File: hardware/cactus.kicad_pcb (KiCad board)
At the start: 2 copper layers, 76.5 x 38.1 mm, 25 parts, among them SW1 SW_Push, U1 WeMos_Battery_Shield, U2 WeMos_D1_mini, U3 74HC595, U4 Si7021_breakout

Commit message: [bug] Remove extra via in R2. Fixed #10
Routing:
- net Net-(D2-Pad2): vias 2 -> 1
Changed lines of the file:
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@@
     (thickness 1.6)
     (drawings 36)
-    (tracks 179)
+    (tracks 178)
     (zones 0)
     (modules 25)
@@
   (layers
     (0 F.Cu signal)
-    (31 B.Cu signal hide)
-    (32 B.Adhes user hide)
+    (31 B.Cu signal)
+    (32 B.Adhes user)
     (33 F.Adhes user)
-    (34 B.Paste user hide)
+    (34 B.Paste user)
     (35 F.Paste user)
-    (36 B.SilkS user hide)
+    (36 B.SilkS user)
     (37 F.SilkS user)
-    (38 B.Mask user hide)
-    (39 F.Mask user hide)
-    (40 Dwgs.User user hide)
-    (41 Cmts.User user hide)
+    (38 B.Mask user)
+    (39 F.Mask user)
+    (40 Dwgs.User user)
+    (41 Cmts.User user)
     (42 Eco1.User user)
     (43 Eco2.User user)
@@
   (segment (start 151.511 55.499) (end 151.638 55.626) (width 0.25) (layer F.Cu) (net 5))
   (segment (start 151.511 54.102) (end 151.511 55.499) (width 0.25) (layer F.Cu) (net 5))
-  (via (at 151.62 56.896) (size 0.8) (drill 0.4) (layers F.Cu B.Cu) (net 5))
   (segment (start 151.638 56.878) (end 151.62 56.896) (width 0.25) (layer B.Cu) (net 5))
   (segment (start 151.638 55.626) (end 151.638 56.878) (width 0.25) (layer B.Cu) (net 5))
@@
     (connect_pads (clearance 0.508))
     (min_thickness 0.254)
-    (fill (arc_segments 16) (thermal_gap 0.508) (thermal_bridge_width 0.508))
+    (fill yes (arc_segments 16) (thermal_gap 0.508) (thermal_bridge_width 0.508))
     (polygon
       (pts
@@
     (connect_pads (clearance 0.508))
     (min_thickness 0.254)
-    (fill (arc_segments 16) (thermal_gap 0.508) (thermal_bridge_width 0.508))
+    (fill yes (arc_segments 16) (thermal_gap 0.508) (thermal_bridge_width 0.508))
     (polygon
       (pts

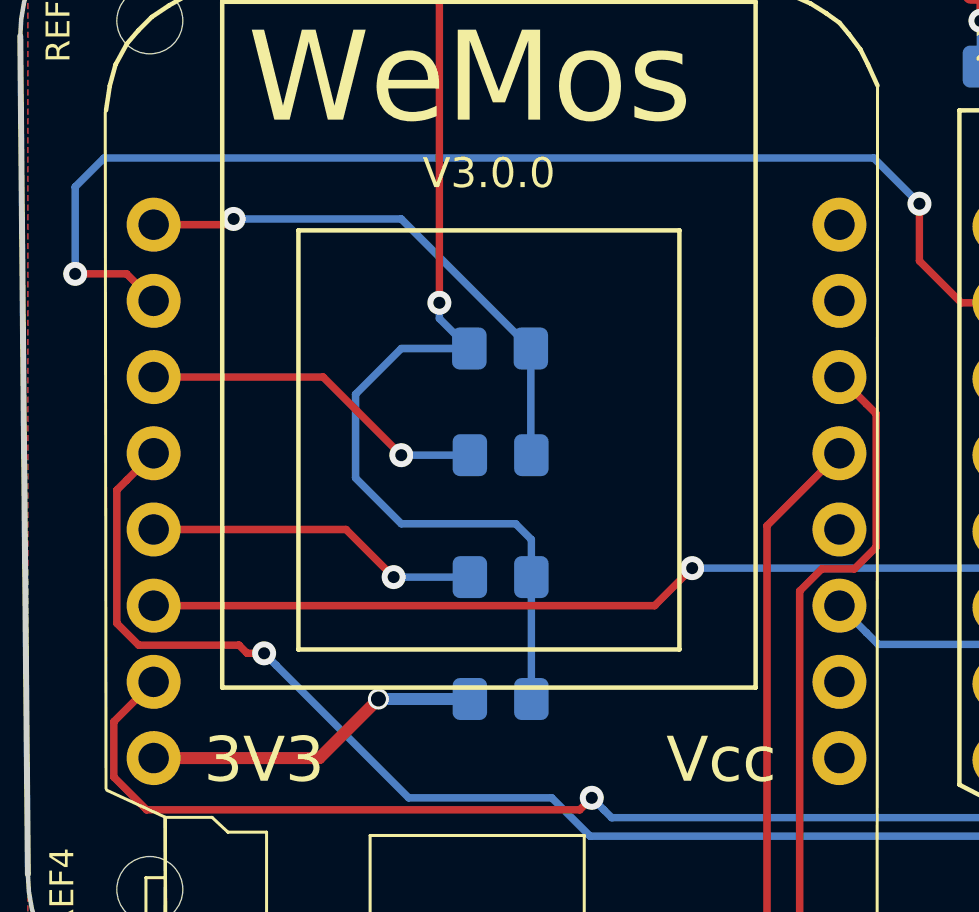
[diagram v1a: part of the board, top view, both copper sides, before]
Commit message: [footprint] Add more pin notes on silkscreen
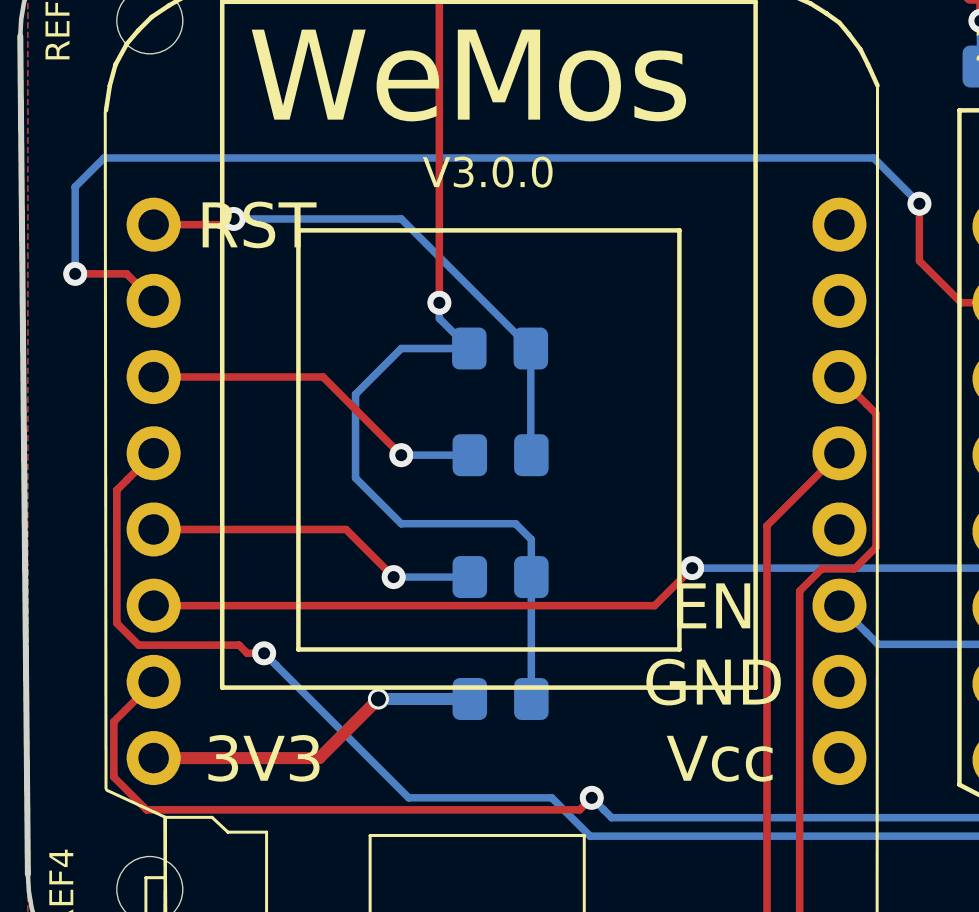
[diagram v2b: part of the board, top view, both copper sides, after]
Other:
- board text added: "EN"
- board text added: "RST"
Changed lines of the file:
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@@
   (general
     (thickness 1.6)
-    (drawings 36)
+    (drawings 39)
     (tracks 178)
     (zones 0)
@@
   (layers
     (0 F.Cu signal)
-    (31 B.Cu signal)
-    (32 B.Adhes user)
+    (31 B.Cu signal hide)
+    (32 B.Adhes user hide)
     (33 F.Adhes user)
-    (34 B.Paste user)
+    (34 B.Paste user hide)
     (35 F.Paste user)
-    (36 B.SilkS user)
+    (36 B.SilkS user hide)
     (37 F.SilkS user)
-    (38 B.Mask user)
+    (38 B.Mask user hide)
     (39 F.Mask user)
     (40 Dwgs.User user)
-    (41 Cmts.User user)
+    (41 Cmts.User user hide)
     (42 Eco1.User user)
     (43 Eco2.User user)
     (44 Edge.Cuts user)
     (45 Margin user)
-    (46 B.CrtYd user)
+    (46 B.CrtYd user hide)
     (47 F.CrtYd user)
-    (48 B.Fab user)
+    (48 B.Fab user hide)
     (49 F.Fab user)
   )
@@
     (pad 1 np_thru_hole circle (at 0 0) (size 2.2 2.2) (drill 2.2) (layers *.Cu *.Mask))
   )
+  (gr_text RST (at 121.92 62.23) (layer F.SilkS)
+    (effects (font (size 1.5 1.5) (thickness 0.1)))
+  )
+  (gr_text EN (at 137.16 74.93) (layer F.SilkS)
+    (effects (font (size 1.5 1.5) (thickness 0.1)))
+  )
+  (gr_text GND (at 137.16 77.47) (layer F.SilkS)
+    (effects (font (size 1.5 1.5) (thickness 0.1)))
+  )
   (gr_text SW1 (at 177.3936 53.2384) (layer B.SilkS)

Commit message: chore: update KiCad6 and ruby gems on Monterey
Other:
- net class Default removed
- net class Power removed
